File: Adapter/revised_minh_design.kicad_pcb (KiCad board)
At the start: 4 copper layers, 96 x 43.9 mm, 40 parts, among them J1 Conn_01x03_Male, J2 Conn_02x08_Odd_Even, J3 Conn_02x08_Odd_Even, J4 Conn_02x08_Odd_Even, J5 Conn_01x02_Male, U1 ESP32-DevKit-C, U2 LM7805_TO220, U3 MCP1754S-3302xCB, U4 MCP1825S-3.3V, U5 MCP1501-33xSN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

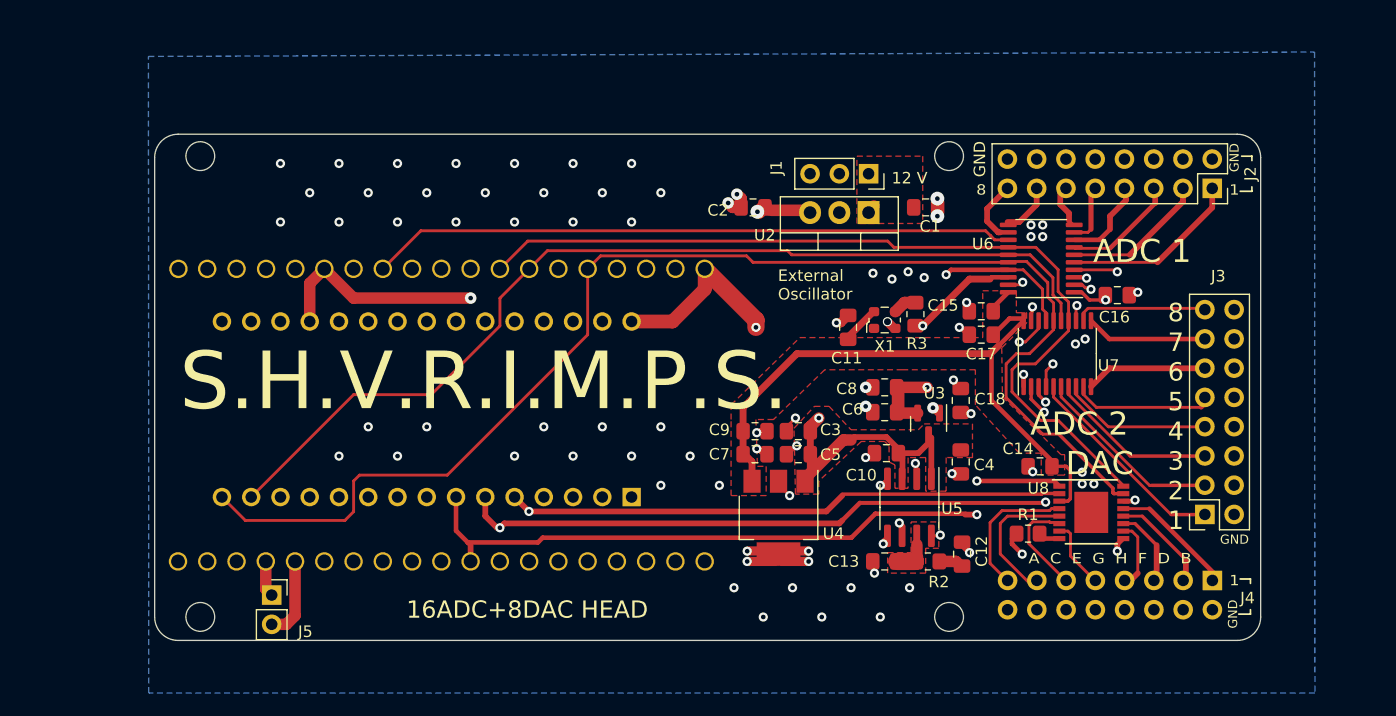
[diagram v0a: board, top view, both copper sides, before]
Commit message: adapter board 4 layers
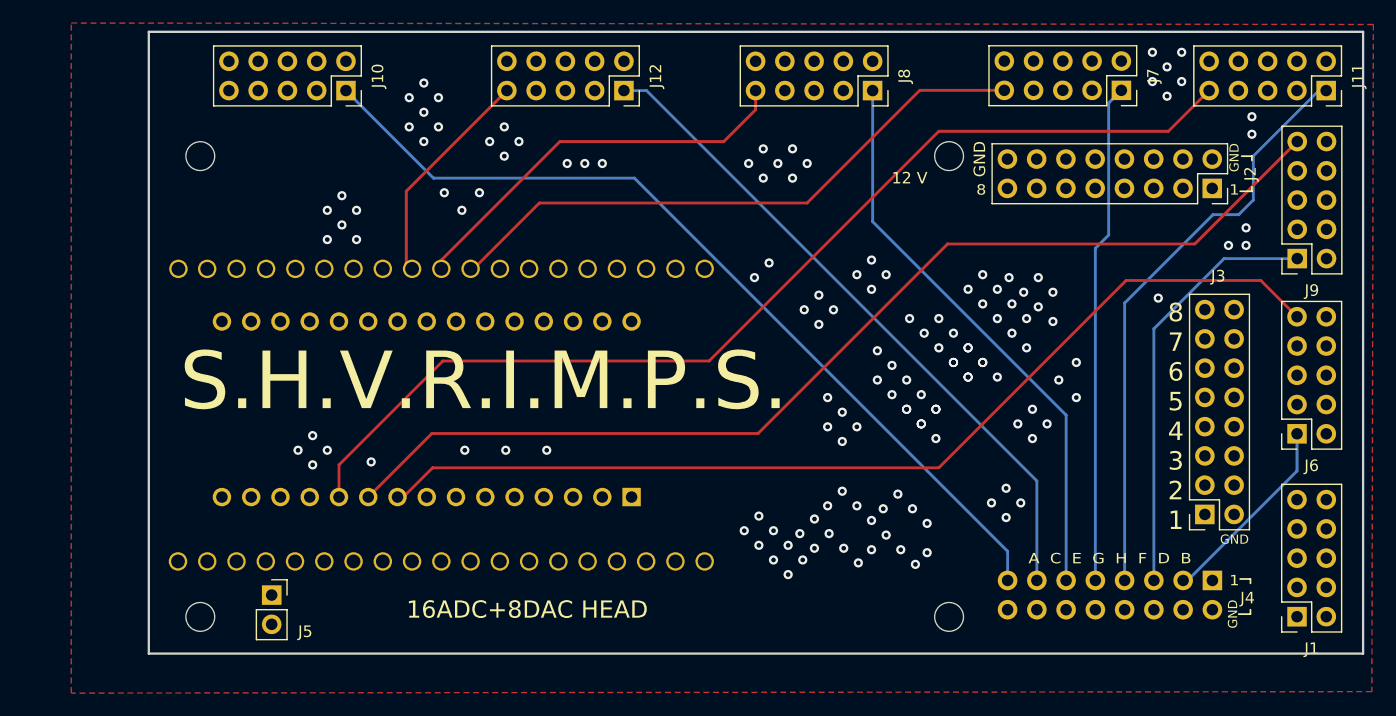
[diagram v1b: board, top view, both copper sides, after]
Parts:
- removed C1, C11, C15, C16, C17, C18, C2, C4, C5, C6, C7: 0.1uF, Capacitor_SMD:C_0805_2012Metric_Pad1.18x1.45mm_HandSolder
- removed C10, C12: 2.2uF, Capacitor_SMD:C_0805_2012Metric_Pad1.18x1.45mm_HandSolder
- removed C13: 1nF, Capacitor_SMD:C_0805_2012Metric_Pad1.18x1.45mm_HandSolder
- removed C14: 1uF, Capacitor_SMD:C_0805_2012Metric_Pad1.18x1.45mm_HandSolder
- removed C3, C8, C9: 10uF, Capacitor_SMD:C_0805_2012Metric_Pad1.18x1.45mm_HandSolder
- removed R1, R3: 0, Resistor_SMD:R_0805_2012Metric_Pad1.20x1.40mm_HandSolder
- removed R2: 50, Resistor_SMD:R_0805_2012Metric_Pad1.20x1.40mm_HandSolder
- removed U2: LM7805_TO220, Package_TO_SOT_THT:TO-220-3_Vertical
- removed U3: MCP1754S-3302xCB, Package_TO_SOT_SMD:SOT-23
- removed U4: MCP1825S-3.3V, Package_TO_SOT_SMD:SOT-223-3_TabPin2
- removed U5: MCP1501-33xSN, Package_SO:SOIC-8_3.9x4.9mm_P1.27mm
- removed U6, U7: MCP3464R, Package_SO:TSSOP-20_4.4x6.5mm_P0.65mm
- removed U8: DAC8568IAPW, Package_SO:TSSOP-16-1EP_4.4x5mm_P0.65mm
- removed X1: ECS-2520MVLC-049-BN-TR, Oscillator:Oscillator_SMD_ECS_2520MV-xxx-xx-4Pin_2.5x2.0mm
- added J10: Conn_02x05_Odd_Even, Connector_PinSocket_2.54mm:PinSocket_2x05_P2.54mm_Vertical, F.Cu at (66.6, 34.3)
- added J11: Conn_02x05_Odd_Even, Connector_PinSocket_2.54mm:PinSocket_2x05_P2.54mm_Vertical, F.Cu at (151.7, 34.3)
- added J12: Conn_02x05_Odd_Even, Connector_PinSocket_2.54mm:PinSocket_2x05_P2.54mm_Vertical, F.Cu at (90.8, 34.3)
- added J6: Conn_02x05_Odd_Even, Connector_PinSocket_2.54mm:PinSocket_2x05_P2.54mm_Vertical, F.Cu at (149.2, 64.1)
- added J7: Conn_02x05_Odd_Even, Connector_PinSocket_2.54mm:PinSocket_2x05_P2.54mm_Vertical, F.Cu at (134.0, 34.3)
- added J8: Conn_02x05_Odd_Even, Connector_PinSocket_2.54mm:PinSocket_2x05_P2.54mm_Vertical, F.Cu at (112.4, 34.3)
- added J9: Conn_02x05_Odd_Even, Connector_PinSocket_2.54mm:PinSocket_2x05_P2.54mm_Vertical, F.Cu at (149.2, 48.9)
- J1: value Conn_01x03_Male -> Conn_02x05_Odd_Even; footprint Connector_PinSocket_2.54mm:PinSocket_1x03_P2.54mm_Vertical -> Connector_PinSocket_2.54mm:PinSocket_2x05_P2.54mm_Vertical
- moved J1 53.5 mm to (149.2, 80.0), turned to 180 degrees
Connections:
- A1 pad 1: RX -> unconnected-(A1-Pad1)
- A1 pad 10: unconnected-(A1-Pad10) -> ENA6
- A1 pad 11: unconnected-(A1-Pad11) -> ENA5
- A1 pad 14: SI -> unconnected-(A1-Pad14)
- A1 pad 15: SO -> unconnected-(A1-Pad15)
- A1 pad 16: SK -> unconnected-(A1-Pad16)
- A1 pad 19: MDAT -> unconnected-(A1-Pad19)
- A1 pad 2: TX -> unconnected-(A1-Pad2)
- A1 pad 20: ~{ADC2_CS} -> unconnected-(A1-Pad20)
- A1 pad 21: ~{ADC1_CS} -> unconnected-(A1-Pad21)
- A1 pad 22: unconnected-(A1-Pad22) -> ENA1
- A1 pad 23: unconnected-(A1-Pad23) -> ENA2
- A1 pad 24: unconnected-(A1-Pad24) -> ENA3
- A1 pad 25: unconnected-(A1-Pad25) -> ENA4
- A1 pad 30: +5V -> unconnected-(A1-Pad30)
- A1 pad 5: ~{DAC_CS} -> unconnected-(A1-Pad5)
- A1 pad 6: ~{CLR} -> unconnected-(A1-Pad6)
- A1 pad 7: LDAC -> unconnected-(A1-Pad7)
- A1 pad 8: unconnected-(A1-Pad8) -> ENA8
- A1 pad 9: unconnected-(A1-Pad9) -> ENA7
- J1 pad 1: +12V -> VoutB
- J1 pad 3: Earth -> unconnected-(J1-Pad3)
- U1 pad 15: TX -> unconnected-(U1-Pad15)
- U1 pad 16: RX -> unconnected-(U1-Pad16)
- U1 pad 24: unconnected-(U1-Pad24) -> ENA1
- U1 pad 25: MDAT -> unconnected-(U1-Pad25)
- U1 pad 26: ~{ADC2_CS} -> unconnected-(U1-Pad26)
- U1 pad 27: ~{ADC1_CS} -> unconnected-(U1-Pad27)
- U1 pad 28: unconnected-(U1-Pad28) -> ENA2
- U1 pad 29: unconnected-(U1-Pad29) -> ENA3
- U1 pad 30: unconnected-(U1-Pad30) -> ENA4
- U1 pad 31: SK -> unconnected-(U1-Pad31)
- U1 pad 32: SI -> unconnected-(U1-Pad32)
- U1 pad 34: SO -> unconnected-(U1-Pad34)
- U1 pad 38: +5V -> unconnected-(U1-Pad38)
- U1 pad 4: unconnected-(U1-Pad4) -> ENA8
- U1 pad 5: unconnected-(U1-Pad5) -> ENA7
- U1 pad 7: ~{DAC_CS} -> unconnected-(U1-Pad7)
- U1 pad 8: ~{CLR} -> unconnected-(U1-Pad8)
- U1 pad 9: LDAC -> unconnected-(U1-Pad9)
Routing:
- net SO: track 114.4 -> 0.00 mm
- net ENA7: track 0.00 -> 106.6 mm
- net SK: track 105.7 -> 0.00 mm
- net ENA8: track 0.00 -> 96.3 mm
- net ENA6: track 0.00 -> 93.4 mm
- net ENA5: track 0.00 -> 91.8 mm
- net SI: track 85.6 -> 0.00 mm
- net MDAT: track 75.7 -> 0.00 mm, vias 2 -> 0
- net ~{ADC2_CS}: track 74.3 -> 0.00 mm, vias 1 -> 0
- net ADC1_6: track 3.84 -> 78.1 mm
- net ADC1_5: track 5.37 -> 78.5 mm
- net VoutA: track 12.5 -> 76.5 mm
- net ~{CLR}: track 63.9 -> 0.00 mm, vias 3 -> 0
- net +5V: track 62.6 -> 0.00 mm, vias 3 -> 0
- net LDAC: track 61.7 -> 0.00 mm, vias 2 -> 0
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- added copper zone on F.Cu, net Earth
- added copper zone on In2.Cu, net Earth
- removed copper zone on F.Cu, net +12V
- removed copper zone on In2.Cu, net +12V
- removed copper zone on F.Cu, net +3.3VDAC
- removed copper zone on In2.Cu, net +3.3VDAC
- removed copper zone on F.Cu, net +3V3
- removed copper zone on F.Cu, net +5V
- removed copper zone on In2.Cu, net +5V
- removed copper zone on B.Cu, net Earth
- removed copper zone on In1.Cu, net Earth
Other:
- board size 96 x 43.9 mm -> 105.4 x 54 mm
- board text removed: "ADC 1"
- board text removed: "ADC 2"
- board text removed: "DAC"
- board text removed: "External Oscillator"
